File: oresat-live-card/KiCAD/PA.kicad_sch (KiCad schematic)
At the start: 33 parts, among them J5 2X1_TH_JUMPER, J9 U.FL, U17 PAT1220-C-3DB, U19 TQP9111, U6 SN74LVC1G32QDBVRQ1, U8 MIC94070YC6-TR

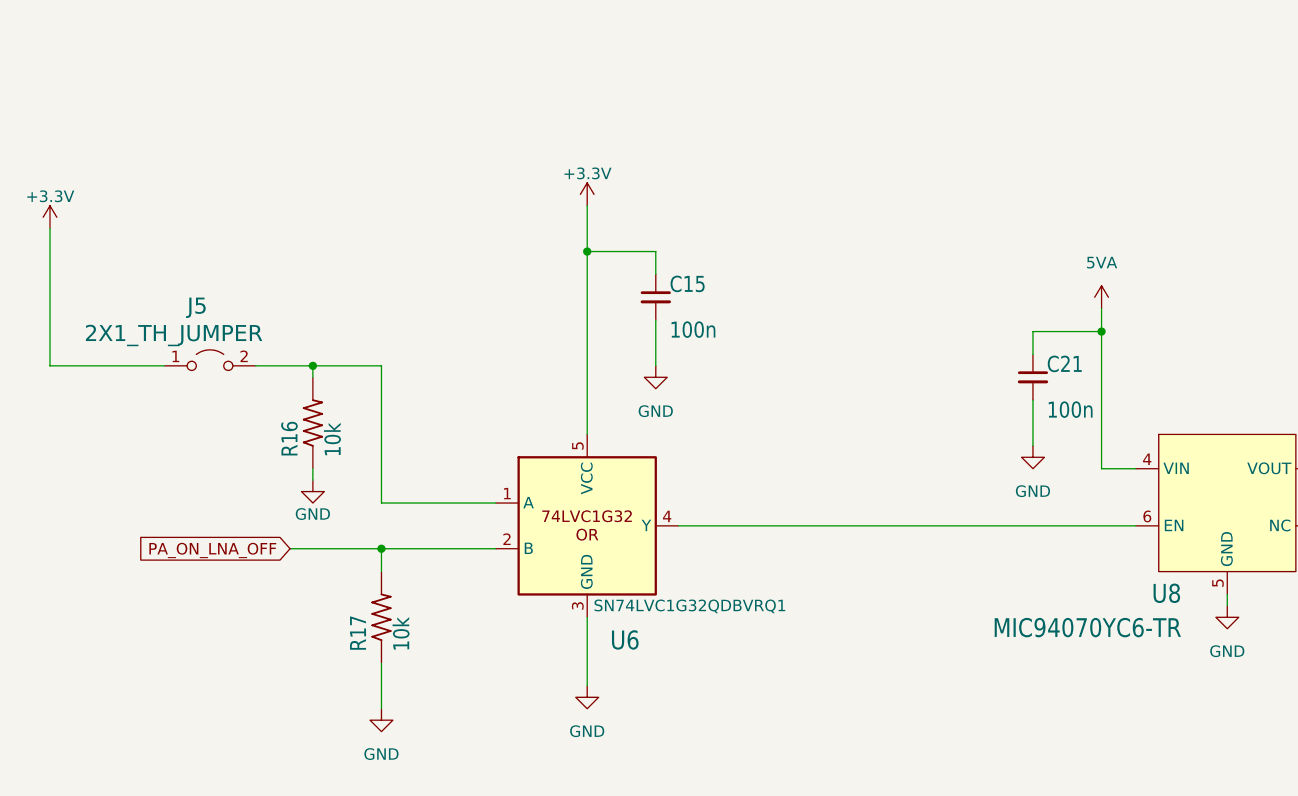
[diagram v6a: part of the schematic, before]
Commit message: Removed or-gate U6 and jumper J5, added Tx/Rx timing delay graphic to schematic, updated all symbols from oresat library, added new components to PCB and started grouping them
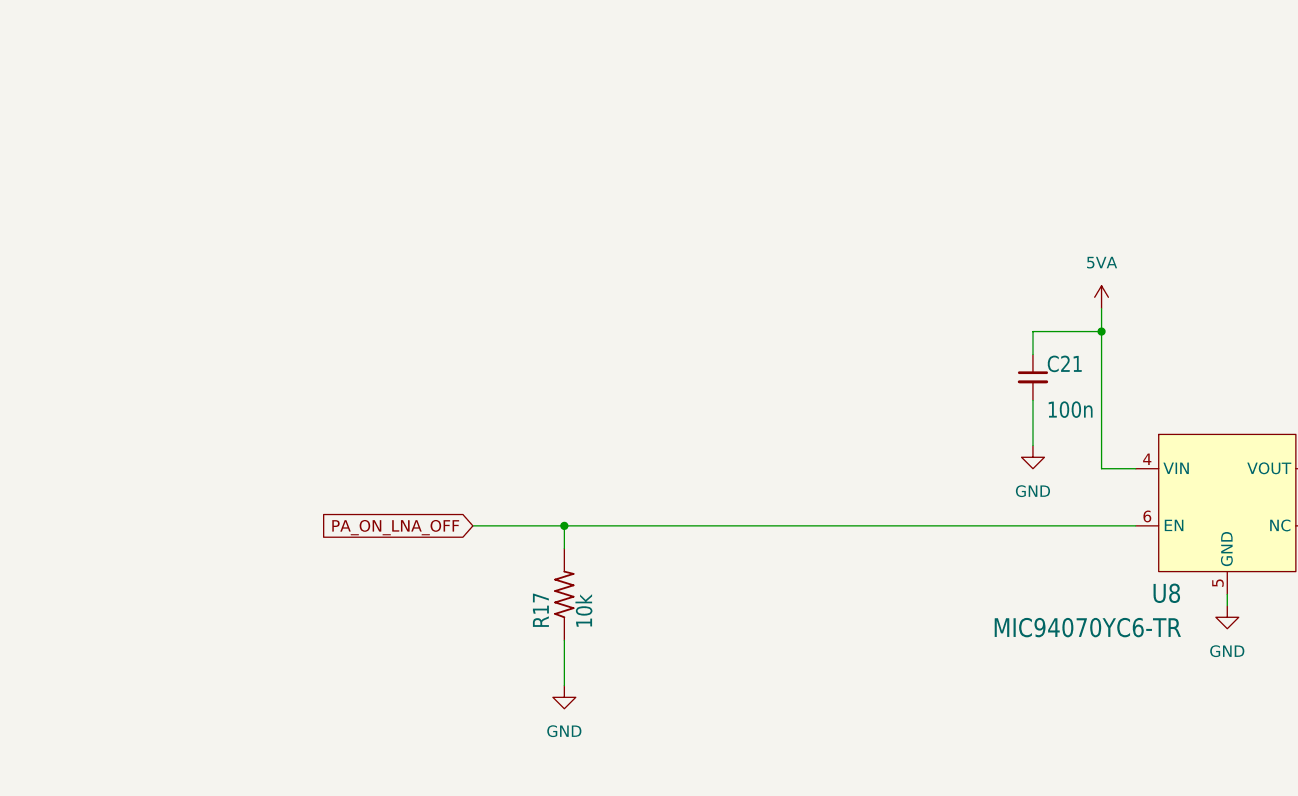
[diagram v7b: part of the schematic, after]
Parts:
- removed C15: 100n, Resistor_SMD:R_0603_1608Metric, symbol Device:C_Small
- removed J5: 2X1_TH_JUMPER, oresat-live-card:2X1, symbol Jumper:Jumper_2_Open
- removed R16: 10k, Resistor_SMD:R_0603_1608Metric, symbol oresat-passives:R-US
- removed U6: SN74LVC1G32QDBVRQ1, symbol oresat-ics:SN74LVC1G32QDBVRQ1
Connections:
- net PA_ON_LNA_OFF: now also U8.6 (EN)
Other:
- moved on the sheet: R17

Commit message: Changed C118, R124, R125 from 0603 to 0402, starting layout and routing
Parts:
- C47: footprint Resistor_SMD:R_0603_1608Metric -> Capacitor_SMD:C_0402_1005Metric
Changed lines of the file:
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@@
 			)
 		)
-		(property "Footprint" "Resistor_SMD:R_0603_1608Metric"
+		(property "Footprint" "Capacitor_SMD:C_0402_1005Metric"
 			(at 266.7 149.86 0)
 			(effects
